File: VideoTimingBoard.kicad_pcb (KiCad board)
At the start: 2 copper layers, 66 x 38.1 mm, 43 parts, among them U1 MC44144, U2 LM1881, U3 SN74LVC3G04, U4 TLV3502

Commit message: Design complete.
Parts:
- removed G***: LOGO, Footprints:weka_small
- added R0: 0R, Resistor_SMD:R_0603_1608Metric_Pad1.05x0.95mm_HandSolder, F.Cu at (148.8, 97.6)
- added R0: 0R, Resistor_SMD:R_0603_1608Metric_Pad1.05x0.95mm_HandSolder, F.Cu at (161.4, 111.4)
- added R0: 0R, Resistor_SMD:R_0603_1608Metric_Pad1.05x0.95mm_HandSolder, F.Cu at (126.9, 101.0)
- added ~: ~, Footprints:weka, F.Cu at (130.0, 91.8)
- C17: value ~ -> 33uF
- FL1: value ~ -> NFE61PT472C1H9L
- R10: value 10K -> 150R
- U3: value SN74LVC3G04 -> SN74LVC1GU04; footprint Package_SO:Texas_R-PDSO-N5 -> Package_TO_SOT_SMD:SOT-23-5_HandSoldering
- U4: value TLV3502 -> TLV3502AIDCNR; footprint Package_TO_SOT_SMD:SOT-23-8_Handsoldering -> Package_SO:SOIC-8_3.9x4.9mm_P1.27mm
- moved C14 3.48 mm to (175.9, 108.1)
- moved C15 3.48 mm to (174.9, 108.1)
- moved C9 2.33 mm to (155.4, 108.7), turned to 180 degrees
- moved U4 2.06 mm to (170.6, 110.4)
- moved U3 1.35 mm to (146.9, 106.6)
- moved R9 0.89 mm to (164.3, 106.7), turned to 180 degrees
- moved C12 0.63 mm to (151.1, 105.1)
- moved C13 0.63 mm to (150.0, 105.1)
- turned D2 to 0 degrees
- turned R6 to 270 degrees
- turned R7 to 90 degrees
- renumbered REF** to ~
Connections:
- C8 pad 1: /FSC -> /FSC-BIAS
- C8 pad 2: Net-(C8-Pad2) -> /FSC
- C9 pad 1: /4FSC -> /4FSC-BIAS
- C9 pad 2: Net-(C9-Pad2) -> /4FSC
- R4 pad 2: /FSC -> /FSC-BIAS
- R5 pad 1: /FSC -> /FSC-BIAS
- R6 pad 2: /4FSC -> /4FSC-BIAS
- R7 pad 1: /4FSC -> /4FSC-BIAS
- U1 pad 1: Net-(C8-Pad2) -> /FSC
- U1 pad 5: Net-(C9-Pad2) -> /4FSC
- U4 pad 2: /FSC -> /FSC-BIAS
- U4 pad 4: /4FSC -> /4FSC-BIAS
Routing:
- net /4FSC-BIAS: track 0.00 -> 17.4 mm
- net /FSC-BIAS: track 0.00 -> 10.9 mm
- net Net-(C9-Pad2): track 9.76 -> 0.00 mm
- net /FSC: track 31.1 -> 22.7 mm
- net VDD: track 151.4 -> 144.6 mm, vias 4 -> 0
- net /FCLK: track 20.1 -> 25.9 mm
- net /4FSC: track 29.8 -> 26.0 mm
- net GND: track 38.8 -> 35.2 mm, vias 75 -> 61
- net /BURST: track 22.3 -> 20.4 mm
- net Net-(C8-Pad2): track 1.91 -> 0.00 mm
- net Net-(R8-Pad2): track 7.44 -> 8.69 mm
- net /BURST-INV: track 26.0 -> 24.8 mm
- net /4FCLK: track 19.2 -> 19.9 mm
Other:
- board text added: "BURSTP"
- board text added: "CVBS"
- board text removed: "BURST-INV"
- board text removed: "CVBS-CLMP"

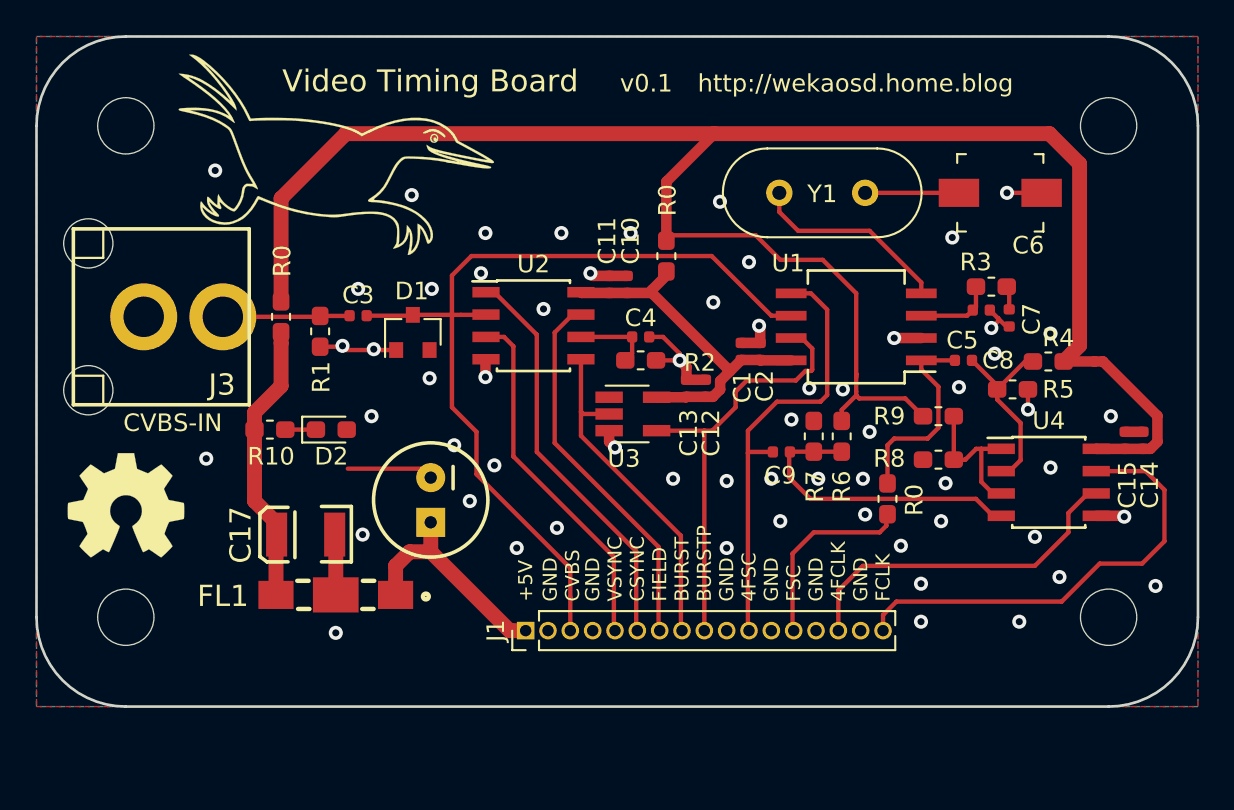
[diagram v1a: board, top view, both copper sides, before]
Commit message: Changed .05" pinheaders to .1" Removed CVBS clamp The MC44144 and LM1881 are separately AC-coupled to the CVBS signal.
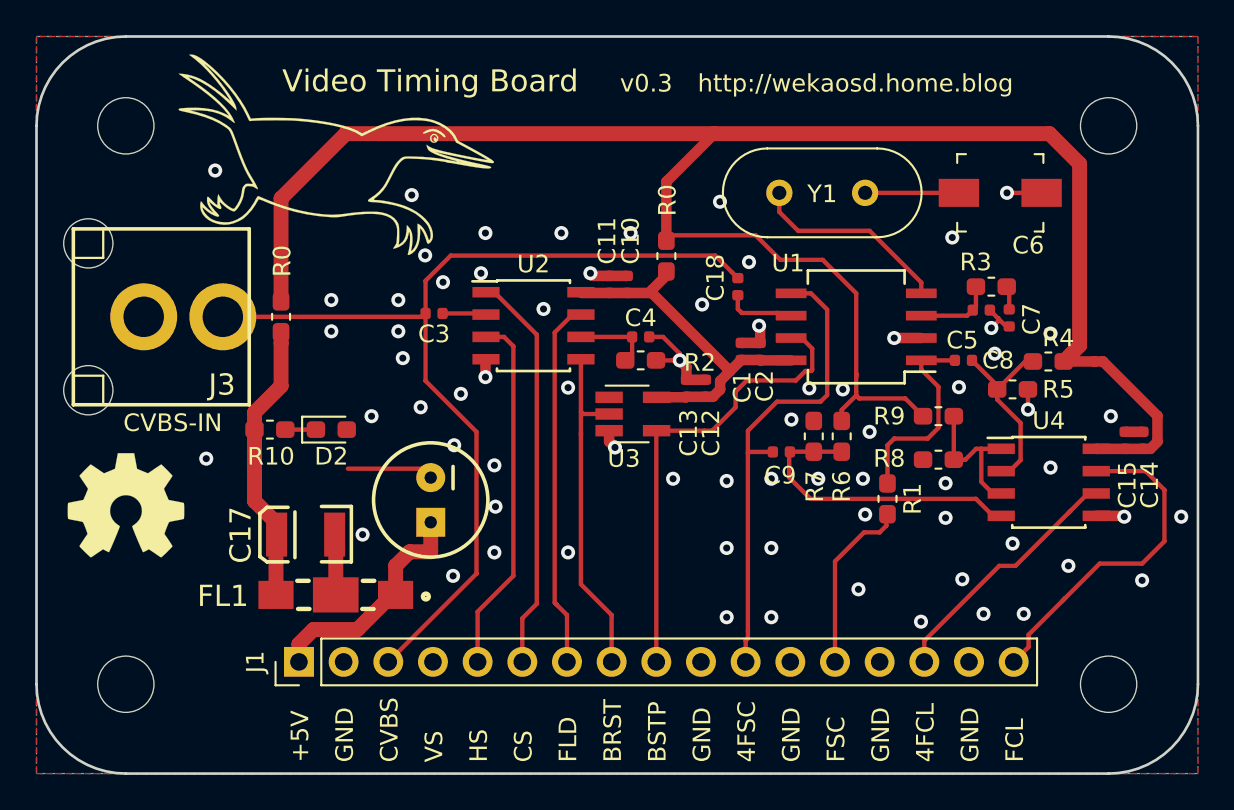
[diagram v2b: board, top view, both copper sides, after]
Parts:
- removed D1: BAT54, Package_TO_SOT_SMD:SOT-23
- removed the R0 at (161.4, 111.4)
- added C18: 0.1uF, Capacitor_SMD:C_0402_1005Metric, F.Cu at (152.9, 99.3)
- J1: footprint Connector_PinHeader_1.27mm:PinHeader_1x17_P1.27mm_Vertical -> Connector_PinHeader_2.54mm:PinHeader_1x17_P2.54mm_Vertical
- R1: value 75R -> 0R
- U4: value TLV3502AIDCNR -> TLV3502
- moved R1 33.6 mm to (161.4, 111.4), turned to 270 degrees
- moved J1 13.0 mm to (128.0, 120.7)
- moved C3 4.32 mm to (135.6, 100.8), turned to 180 degrees
- moved ~ 3.81 mm to (174.0, 121.9)
- moved ~ 3.81 mm to (118.1, 121.9)
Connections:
- C3 pad 1: /CVBS-IN -> Net-(C3-Pad1)
- C3 pad 2: /CVBS-CLAMPED -> /CVBS
- J1 pad 13: /FSC -> /FSC1
- J1 pad 3: /CVBS-CLAMPED -> /CVBS
- J3 pad 1: /CVBS-IN -> /CVBS
- R0 pad 1: VDD -> /FSC
- R0 pad 2: VDD -> /FSC
- R1 pad 1: GND -> /FSC
- R1 pad 2: /CVBS-IN -> /FSC1
- U1 pad 6: /CVBS-CLAMPED -> Net-(C18-Pad2)
- U2 pad 2: /CVBS-CLAMPED -> Net-(C3-Pad1)
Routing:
- net /CVBS: track 0.00 -> 55.4 mm
- net /CVBS-CLAMPED: track 50.9 -> 0.00 mm
- net /FSC: track 22.7 -> 11.6 mm
- net /FSC1: track 0.00 -> 10.2 mm
- net /CVBS-IN: track 7.23 -> 0.00 mm
- net /FCLK: track 25.9 -> 19.3 mm
- net /4FCLK: track 19.9 -> 14.6 mm
- net GND: track 35.2 -> 30.8 mm, vias 61 -> 70
- net Net-(C18-Pad2): track 0.00 -> 3.97 mm
- net Net-(C3-Pad1): track 0.00 -> 2.52 mm
- net /4FSC: track 26.0 -> 27.9 mm
- net /BURST-INV: track 24.8 -> 26.6 mm
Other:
- board size 66 x 38.1 mm -> 66 x 41.9 mm
- board text added: "4FCL"
- board text added: "BRST"
- board text added: "BSTP"
- board text added: "CS"
- board text added: "FCL"
- board text added: "FLD"
- board text added: "HS"
- board text added: "VS"
- board text added: "v0.3"
- board text removed: "4FCLK"
- board text removed: "BURST"
- board text removed: "BURSTP"
- board text removed: "CSYNC"
- board text removed: "FCLK"
- board text removed: "FIELD"
- board text removed: "VSYNC"
- board text removed: "v0.1"

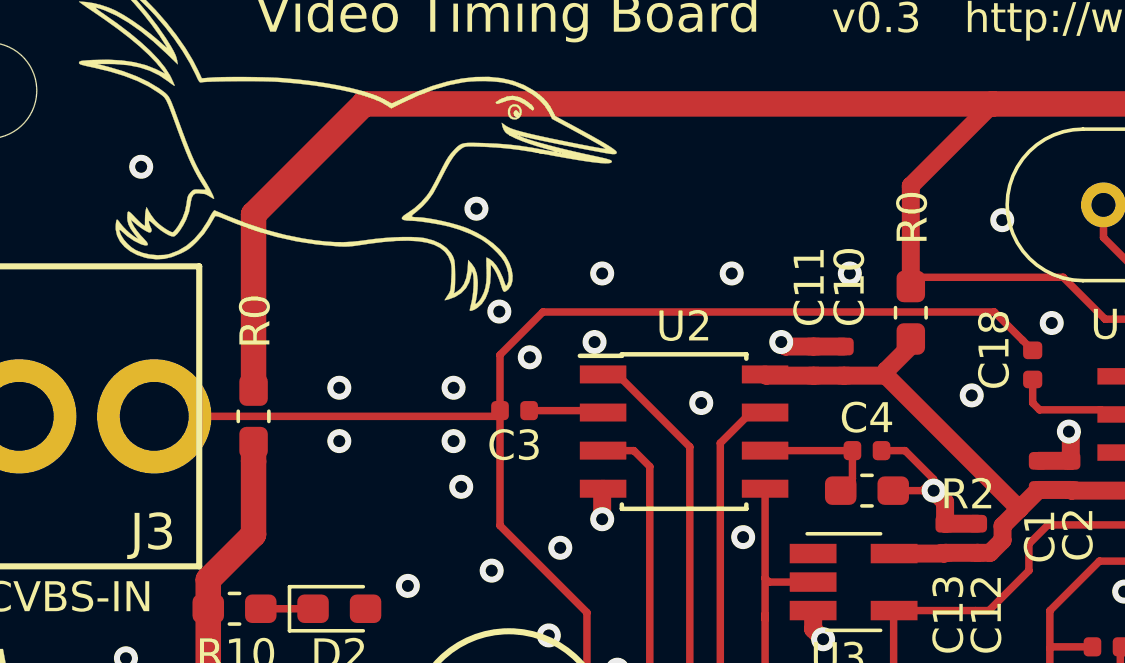
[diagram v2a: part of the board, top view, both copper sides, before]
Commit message: Changed jumpers
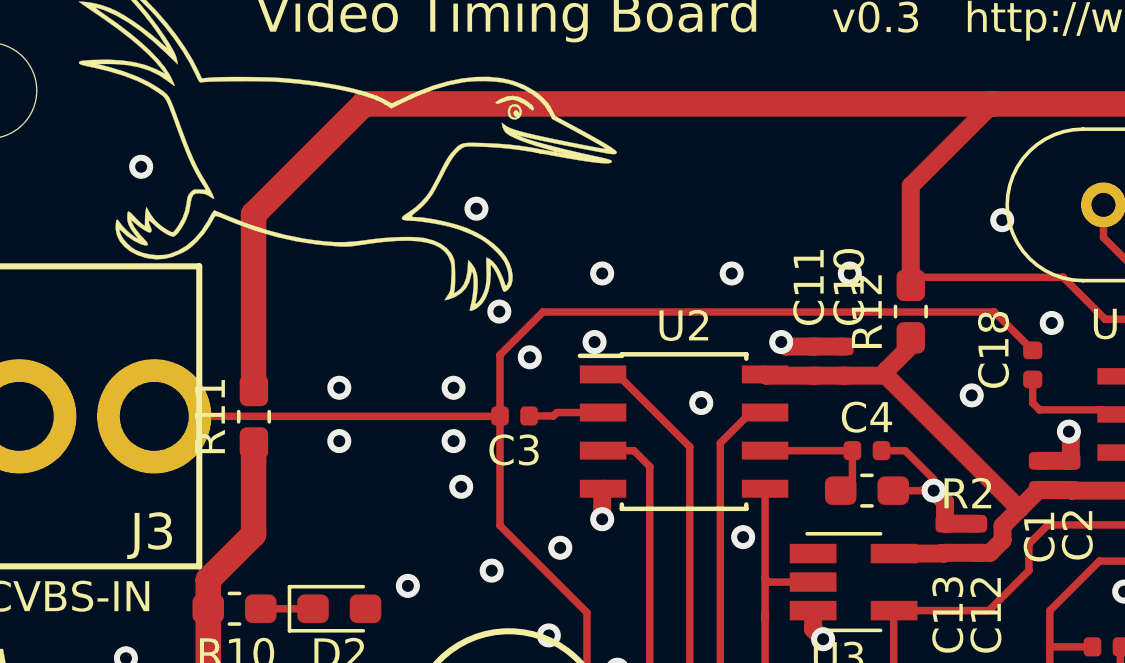
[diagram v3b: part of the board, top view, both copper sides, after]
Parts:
- removed R0 (x2): 0R, Resistor_SMD:R_0603_1608Metric_Pad1.05x0.95mm_HandSolder
- added R11: 0R, Resistor_SMD:R_0603_1608Metric_Pad1.05x0.95mm_HandSolder, F.Cu at (126.9, 101.0)
- added R12: R0, Resistor_SMD:R_0603_1608Metric_Pad1.05x0.95mm_HandSolder, F.Cu at (148.8, 97.5)
- moved C3 0.18 mm to (135.6, 101.0)
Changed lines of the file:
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@@
     (thickness 1.6)
     (drawings 31)
-    (tracks 320)
+    (tracks 322)
     (zones 0)
     (modules 45)
@@
     )
   )
-  (module Resistor_SMD:R_0603_1608Metric_Pad1.05x0.95mm_HandSolder (layer F.Cu)
-    (at 148.844 97.5754 90)
-    (descr "Resistor SMD 0603 (1608 Metric), square (rectangular) end terminal, IPC_7351 nominal with elongated pad for handsoldering. (Body size source: http://www.tortai-tech.com/upload/download/2011102023233369053.pdf), generated with kicad-footprint-generator")
-    (tags "resistor handsolder")
-    (attr smd)
-    (fp_text reference R0 (at 3.175 0.0635 90) (layer F.SilkS)
-      (effects (font (size 1 1) (thickness 0.15)))
-    )
-    (fp_text value 0R (at 2.8334 0 90) (layer F.Fab)
-      (effects (font (size 1 1) (thickness 0.15)))
-    )
-    (fp_line (start -0.8 0.4) (end -0.8 -0.4) (layer F.Fab) (width 0.1))
-    (fp_line (start -0.8 -0.4) (end 0.8 -0.4) (layer F.Fab) (width 0.1))
-    (fp_line (start 0.8 -0.4) (end 0.8 0.4) (layer F.Fab) (width 0.1))
-    (fp_line (start 0.8 0.4) (end -0.8 0.4) (layer F.Fab) (width 0.1))
-    (fp_line (start -0.171267 -0.51) (end 0.171267 -0.51) (layer F.SilkS) (width 0.12))
-    (fp_line (start -0.171267 0.51) (end 0.171267 0.51) (layer F.SilkS) (width 0.12))
-    (fp_line (start -1.65 0.73) (end -1.65 -0.73) (layer F.CrtYd) (width 0.05))
-    (fp_line (start -1.65 -0.73) (end 1.65 -0.73) (layer F.CrtYd) (width 0.05))
-    (fp_line (start 1.65 -0.73) (end 1.65 0.73) (layer F.CrtYd) (width 0.05))
-    (fp_line (start 1.65 0.73) (end -1.65 0.73) (layer F.CrtYd) (width 0.05))
-    (fp_text user %R (at 0 0 90) (layer F.Fab)
-      (effects (font (size 0.4 0.4) (thickness 0.06)))
-    )
-    (pad 1 smd roundrect (at -0.875 0 90) (size 1.05 0.95) (layers F.Cu F.Paste F.Mask) (roundrect_rratio 0.25)
-      (net 9 /FSC))
-    (pad 2 smd roundrect (at 0.875 0 90) (size 1.05 0.95) (layers F.Cu F.Paste F.Mask) (roundrect_rratio 0.25)
-      (net 9 /FSC))
-    (model ${KISYS3DMOD}/Resistor_SMD.3dshapes/R_0603_1608Metric.wrl
-      (at (xyz 0 0 0))
-      (scale (xyz 1 1 1))
-      (rotate (xyz 0 0 0))
-    )
-  )
   (module Capacitor_SMD:C_0402_1005Metric (layer F.Cu)
     (at 168.3385 101.092 90)
@@
   )
   (module Capacitor_SMD:C_0402_1005Metric (layer F.Cu)
-    (at 135.636 100.838 180)
+    (at 135.636 101.0158 180)
     (descr "Capacitor SMD 0402 (1005 Metric), square (rectangular) end terminal, IPC_7351 nominal, (Body size source: http://www.tortai-tech.com/upload/download/2011102023233369053.pdf), generated with kicad-footprint-generator")
     (tags capacitor)
@@
       (xy -0.621095 -2.086445) (xy -0.537275 -2.531069) (xy -0.453454 -2.975693) (xy 0.471994 -2.975693)
       (xy 0.555814 -2.531069)) (layer F.SilkS) (width 0.01))
-  )
-  (module Resistor_SMD:R_0603_1608Metric_Pad1.05x0.95mm_HandSolder (layer F.Cu)
-    (at 126.9365 101.0285 90)
-    (descr "Resistor SMD 0603 (1608 Metric), square (rectangular) end terminal, IPC_7351 nominal with elongated pad for handsoldering. (Body size source: http://www.tortai-tech.com/upload/download/2011102023233369053.pdf), generated with kicad-footprint-generator")
-    (tags "resistor handsolder")
-    (attr smd)
-    (fp_text reference R0 (at 3.175 0.0635 90) (layer F.SilkS)
-      (effects (font (size 1 1) (thickness 0.15)))
-    )
-    (fp_text value 0R (at 2.7305 0.0635 90) (layer F.Fab)
-      (effects (font (size 1 1) (thickness 0.15)))
-    )
-    (fp_text user %R (at 0 0 90) (layer F.Fab)
-      (effects (font (size 0.4 0.4) (thickness 0.06)))
-    )
-    (fp_line (start 1.65 0.73) (end -1.65 0.73) (layer F.CrtYd) (width 0.05))
-    (fp_line (start 1.65 -0.73) (end 1.65 0.73) (layer F.CrtYd) (width 0.05))
-    (fp_line (start -1.65 -0.73) (end 1.65 -0.73) (layer F.CrtYd) (width 0.05))
-    (fp_line (start -1.65 0.73) (end -1.65 -0.73) (layer F.CrtYd) (width 0.05))
-    (fp_line (start -0.171267 0.51) (end 0.171267 0.51) (layer F.SilkS) (width 0.12))
-    (fp_line (start -0.171267 -0.51) (end 0.171267 -0.51) (layer F.SilkS) (width 0.12))
-    (fp_line (start 0.8 0.4) (end -0.8 0.4) (layer F.Fab) (width 0.1))
-    (fp_line (start 0.8 -0.4) (end 0.8 0.4) (layer F.Fab) (width 0.1))
-    (fp_line (start -0.8 -0.4) (end 0.8 -0.4) (layer F.Fab) (width 0.1))
-    (fp_line (start -0.8 0.4) (end -0.8 -0.4) (layer F.Fab) (width 0.1))
-    (pad 2 smd roundrect (at 0.875 0 90) (size 1.05 0.95) (layers F.Cu F.Paste F.Mask) (roundrect_rratio 0.25)
-      (net 3 VDD))
-    (pad 1 smd roundrect (at -0.875 0 90) (size 1.05 0.95) (layers F.Cu F.Paste F.Mask) (roundrect_rratio 0.25)
-      (net 3 VDD))
-    (model ${KISYS3DMOD}/Resistor_SMD.3dshapes/R_0603_1608Metric.wrl
-      (at (xyz 0 0 0))
-      (scale (xyz 1 1 1))
-      (rotate (xyz 0 0 0))
-    )
   )
   (module Footprints:weka (layer F.Cu)
@@
     (pad 2 smd roundrect (at 0.875 0 270) (size 1.05 0.95) (layers F.Cu F.Paste F.Mask) (roundrect_rratio 0.25)
       (net 26 /FSC1))
+    (model ${KISYS3DMOD}/Resistor_SMD.3dshapes/R_0603_1608Metric.wrl
+      (at (xyz 0 0 0))
+      (scale (xyz 1 1 1))
+      (rotate (xyz 0 0 0))
+    )
+  )
+  (module Resistor_SMD:R_0603_1608Metric_Pad1.05x0.95mm_HandSolder (layer F.Cu)
+    (at 126.9492 101.0412 90)
+    (descr "Resistor SMD 0603 (1608 Metric), square (rectangular) end terminal, IPC_7351 nominal with elongated pad for handsoldering. (Body size source: http://www.tortai-tech.com/upload/download/2011102023233369053.pdf), generated with kicad-footprint-generator")
+    (tags "resistor handsolder")
+    (attr smd)
+    (fp_text reference R11 (at 0 -1.43 90) (layer F.SilkS)
+      (effects (font (size 1 1) (thickness 0.15)))
+    )
+    (fp_text value 0R (at 0 1.43 90) (layer F.Fab)
+      (effects (font (size 1 1) (thickness 0.15)))
+    )
+    (fp_text user %R (at 0 0 90) (layer F.Fab)
+      (effects (font (size 0.4 0.4) (thickness 0.06)))
+    )
+    (fp_line (start 1.65 0.73) (end -1.65 0.73) (layer F.CrtYd) (width 0.05))
+    (fp_line (start 1.65 -0.73) (end 1.65 0.73) (layer F.CrtYd) (width 0.05))
+    (fp_line (start -1.65 -0.73) (end 1.65 -0.73) (layer F.CrtYd) (width 0.05))
+    (fp_line (start -1.65 0.73) (end -1.65 -0.73) (layer F.CrtYd) (width 0.05))
+    (fp_line (start -0.171267 0.51) (end 0.171267 0.51) (layer F.SilkS) (width 0.12))
+    (fp_line (start -0.171267 -0.51) (end 0.171267 -0.51) (layer F.SilkS) (width 0.12))
+    (fp_line (start 0.8 0.4) (end -0.8 0.4) (layer F.Fab) (width 0.1))
+    (fp_line (start 0.8 -0.4) (end 0.8 0.4) (layer F.Fab) (width 0.1))
+    (fp_line (start -0.8 -0.4) (end 0.8 -0.4) (layer F.Fab) (width 0.1))
+    (fp_line (start -0.8 0.4) (end -0.8 -0.4) (layer F.Fab) (width 0.1))
+    (pad 2 smd roundrect (at 0.875 0 90) (size 1.05 0.95) (layers F.Cu F.Paste F.Mask) (roundrect_rratio 0.25)
+      (net 3 VDD))
+    (pad 1 smd roundrect (at -0.875 0 90) (size 1.05 0.95) (layers F.Cu F.Paste F.Mask) (roundrect_rratio 0.25)
+      (net 3 VDD))
+    (model ${KISYS3DMOD}/Resistor_SMD.3dshapes/R_0603_1608Metric.wrl
+      (at (xyz 0 0 0))
+      (scale (xyz 1 1 1))
+      (rotate (xyz 0 0 0))
+    )
+  )
+  (module Resistor_SMD:R_0603_1608Metric_Pad1.05x0.95mm_HandSolder (layer F.Cu)
+    (at 148.844 97.536 90)
+    (descr "Resistor SMD 0603 (1608 Metric), square (rectangular) end terminal, IPC_7351 nominal with elongated pad for handsoldering. (Body size source: http://www.tortai-tech.com/upload/download/2011102023233369053.pdf), generated with kicad-footprint-generator")
+    (tags "resistor handsolder")
+    (attr smd)
+    (fp_text reference R12 (at 0 -1.43 90) (layer F.SilkS)
+      (effects (font (size 1 1) (thickness 0.15)))
+    )
+    (fp_text value R0 (at 0 1.43 90) (layer F.Fab)
+      (effects (font (size 1 1) (thickness 0.15)))
+    )
+    (fp_line (start -0.8 0.4) (end -0.8 -0.4) (layer F.Fab) (width 0.1))
+    (fp_line (start -0.8 -0.4) (end 0.8 -0.4) (layer F.Fab) (width 0.1))
+    (fp_line (start 0.8 -0.4) (end 0.8 0.4) (layer F.Fab) (width 0.1))
+    (fp_line (start 0.8 0.4) (end -0.8 0.4) (layer F.Fab) (width 0.1))
+    (fp_line (start -0.171267 -0.51) (end 0.171267 -0.51) (layer F.SilkS) (width 0.12))
+    (fp_line (start -0.171267 0.51) (end 0.171267 0.51) (layer F.SilkS) (width 0.12))
+    (fp_line (start -1.65 0.73) (end -1.65 -0.73) (layer F.CrtYd) (width 0.05))
+    (fp_line (start -1.65 -0.73) (end 1.65 -0.73) (layer F.CrtYd) (width 0.05))
+    (fp_line (start 1.65 -0.73) (end 1.65 0.73) (layer F.CrtYd) (width 0.05))
+    (fp_line (start 1.65 0.73) (end -1.65 0.73) (layer F.CrtYd) (width 0.05))
+    (fp_text user %R (at 0 0 90) (layer F.Fab)
+      (effects (font (size 0.4 0.4) (thickness 0.06)))
+    )
+    (pad 1 smd roundrect (at -0.875 0 90) (size 1.05 0.95) (layers F.Cu F.Paste F.Mask) (roundrect_rratio 0.25)
+      (net 3 VDD))
+    (pad 2 smd roundrect (at 0.875 0 90) (size 1.05 0.95) (layers F.Cu F.Paste F.Mask) (roundrect_rratio 0.25)
+      (net 3 VDD))
     (model ${KISYS3DMOD}/Resistor_SMD.3dshapes/R_0603_1608Metric.wrl
       (at (xyz 0 0 0))
@@
   (segment (start 123.626 101.0285) (end 134.9605 101.0285) (width 0.25) (layer F.Cu) (net 23))
   (segment (start 138.524 100.838) (end 138.5875 100.9015) (width 0.25) (layer F.Cu) (net 24))
-  (segment (start 136.121 100.838) (end 138.524 100.838) (width 0.25) (layer F.Cu) (net 24))
+  (segment (start 138.5875 100.9015) (end 137.0457 100.9015) (width 0.25) (layer F.Cu) (net 24))
+  (segment (start 136.9314 101.0158) (end 136.121 101.0158) (width 0.25) (layer F.Cu) (net 24))
+  (segment (start 137.0457 100.9015) (end 136.9314 101.0158) (width 0.25) (layer F.Cu) (net 24))
   (segment (start 155.339 100.965) (end 155.939 100.965) (width 0.25) (layer F.Cu) (net 25))
   (segment (start 155.185499 100.811499) (end 155.339 100.965) (width 0.25) (layer F.Cu) (net 25))
